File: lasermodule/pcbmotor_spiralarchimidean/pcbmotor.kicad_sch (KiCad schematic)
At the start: 1 part, among them J1 Conn_01x03

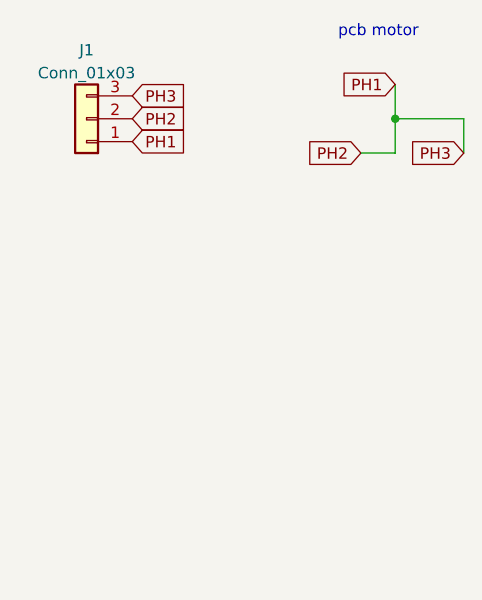
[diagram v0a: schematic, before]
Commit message: added optimized pcbmotor of atomic14
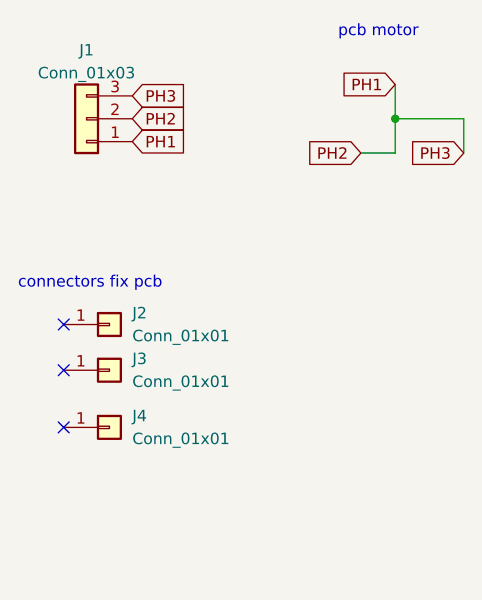
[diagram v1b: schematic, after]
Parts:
- added J2, J3, J4: Conn_01x01, pcbmotor:PinHeader_1x01_P2.54mm_Vertical, symbol Connector_Generic:Conn_01x01
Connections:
- no-connect marks 0 -> 3
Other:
- note added: "connectors fix pcb"
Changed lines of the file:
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@@
   (junction (at 85.09 36.83) (diameter 0) (color 0 0 0 0)
   )
+  (no_connect (at 48.26 59.69))
+  (no_connect (at 48.26 71.12))
+  (no_connect (at 48.26 64.77))
   (wire (pts (xy 81.28 40.64) (xy 85.09 40.64))
     (stroke (width 0) (type default))
@@
   )
   (text "pcb motor" (at 78.74 27.94 0)
+    (effects (font (size 1.27 1.27)) (justify left bottom))
+  )
+  (text "connectors fix pcb" (at 43.18 55.88 0)
     (effects (font (size 1.27 1.27)) (justify left bottom))
   )
@@
         )
       )
+    )
+  )
+  (symbol (lib_id "Connector_Generic:Conn_01x01") (at 53.34 59.69 0) (unit 1)
+    (in_bom yes) (on_board yes) (dnp no) (fields_autoplaced)
+    (property "Reference" "J2" (at 55.88 58.42 0)
+      (effects (font (size 1.27 1.27)) (justify left))
+    )
+    (property "Value" "Conn_01x01" (at 55.88 60.96 0)
+      (effects (font (size 1.27 1.27)) (justify left))
+    )
+    (property "Footprint" "pcbmotor:PinHeader_1x01_P2.54mm_Vertical" (at 53.34 59.69 0)
+      (effects (font (size 1.27 1.27)) hide)
+    )
+    (property "Datasheet" "~" (at 53.34 59.69 0)
+      (effects (font (size 1.27 1.27)) hide)
+    )
+    (pin "1")
+    (instances
+      (project "pcbmotor"
+        (path "/e63e39d7-6ac0-4ffd-8aa3-1841a4541b55"
+          (reference "J2") (unit 1)
+        )
+      )
+    )
+  )
+  (symbol (lib_id "Connector_Generic:Conn_01x01") (at 53.34 64.77 0) (unit 1)
+    (in_bom yes) (on_board yes) (dnp no) (fields_autoplaced)
+    (property "Reference" "J3" (at 55.88 63.5 0)
+      (effects (font (size 1.27 1.27)) (justify left))
+    )
+    (property "Value" "Conn_01x01" (at 55.88 66.04 0)
+      (effects (font (size 1.27 1.27)) (justify left))
+    )
+    (property "Footprint" "pcbmotor:PinHeader_1x01_P2.54mm_Vertical" (at 53.34 64.77 0)
+      (effects (font (size 1.27 1.27)) hide)
+    )
+    (property "Datasheet" "~" (at 53.34 64.77 0)
+      (effects (font (size 1.27 1.27)) hide)
+    )
+    (pin "1")
+    (instances
+      (project "pcbmotor"
+        (path "/e63e39d7-6ac0-4ffd-8aa3-1841a4541b55"
+          (reference "J3") (unit 1)
+        )
+      )
+    )
+  )
+  (symbol (lib_id "Connector_Generic:Conn_01x01") (at 53.34 71.12 0) (unit 1)
+    (in_bom yes) (on_board yes) (dnp no) (fields_autoplaced)
+    (property "Reference" "J4" (at 55.88 69.85 0)
+      (effects (font (size 1.27 1.27)) (justify left))
+    )
+    (property "Value" "Conn_01x01" (at 55.88 72.39 0)
+      (effects (font (size 1.27 1.27)) (justify left))
+    )
+    (property "Footprint" "pcbmotor:PinHeader_1x01_P2.54mm_Vertical" (at 53.34 71.12 0)
+      (effects (font (size 1.27 1.27)) hide)
+    )
+    (property "Datasheet" "~" (at 53.34 71.12 0)
+      (effects (font (size 1.27 1.27)) hide)
+    )
+    (pin "1")
+    (instances
+      (project "pcbmotor"
+        (path "/e63e39d7-6ac0-4ffd-8aa3-1841a4541b55"
+          (reference "J4") (unit 1)
+        )
+      )

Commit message: removed need for screws using pcb pads
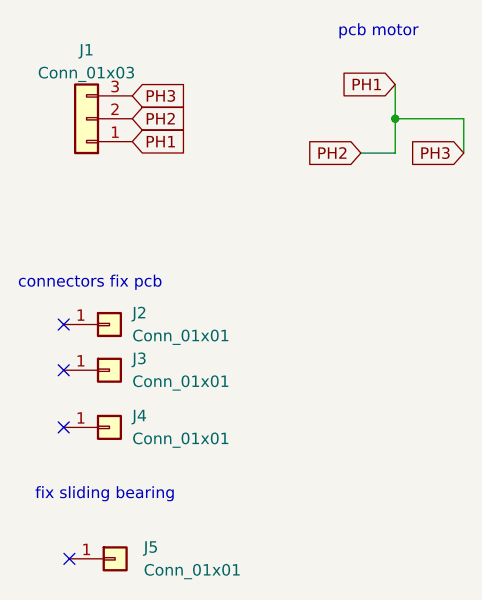
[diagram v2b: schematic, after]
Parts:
- added J5: Conn_01x01, pcbmotor:motorconnector_D8.0mm_Drill4.1mm, symbol Connector_Generic:Conn_01x01
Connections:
- no-connect marks 3 -> 4
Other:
- note added: "fix sliding bearing"
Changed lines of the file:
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@@
   (no_connect (at 48.26 71.12))
   (no_connect (at 48.26 64.77))
+  (no_connect (at 48.895 85.725))
   (wire (pts (xy 81.28 40.64) (xy 85.09 40.64))
     (stroke (width 0) (type default))
@@
   (wire (pts (xy 85.09 36.83) (xy 92.71 36.83))
     (stroke (width 0) (type default))
+  )
+  (text "fix sliding bearing" (at 45.085 79.375 0)
+    (effects (font (size 1.27 1.27)) (justify left bottom))
   )
   (text "pcb motor" (at 78.74 27.94 0)
@@
     )
   )
+  (symbol (lib_id "Connector_Generic:Conn_01x01") (at 53.975 85.725 0) (unit 1)
+    (in_bom yes) (on_board yes) (dnp no) (fields_autoplaced)
+    (property "Reference" "J5" (at 57.15 84.455 0)
+      (effects (font (size 1.27 1.27)) (justify left))
+    )
+    (property "Value" "Conn_01x01" (at 57.15 86.995 0)
+      (effects (font (size 1.27 1.27)) (justify left))
+    )
+    (property "Footprint" "pcbmotor:motorconnector_D8.0mm_Drill4.1mm" (at 53.975 85.725 0)
+      (effects (font (size 1.27 1.27)) hide)
+    )
+    (property "Datasheet" "~" (at 53.975 85.725 0)
+      (effects (font (size 1.27 1.27)) hide)
+    )
+    (pin "1")
+    (instances
+      (project "pcbmotor"
+        (path "/e63e39d7-6ac0-4ffd-8aa3-1841a4541b55"
+          (reference "J5") (unit 1)
+        )
+      )
+    )
+  )
